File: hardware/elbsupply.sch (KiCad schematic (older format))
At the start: 84 parts, among them CON1 AVR-ISP-6, IC1 ATMEGA8-AI, P1 OUT_POS, P2 OUT_GND, P3 POWER_IN, Q1 KST2907A, SW1 SW_L, SW2 SW_R, SW3 SW_OE, SW4 SW_MD, U1 LM393, U2 TPS54331DDA, U3 LT1490, U4 LM358, U5 TS78L05CS, U6 LT3083, U7 LM334

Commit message: changed components to improve loop stability
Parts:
- added C?: 0.1uF, symbol C
- added R?: 10k, symbol R
- C14, C21: value 0.1uF -> 1uF
- C4: value 7pF -> 22pF
- R1: value 102k -> 100k
- R19: value 10k -> 1k
- R21, R7: value 1k -> 10k
- R26: value 68R -> 100R
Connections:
- wire segments 317 -> 324
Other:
- note added: "CC mode comparator\npulls output control voltage to \nGND when current exceeds \nset maximum"
- note added: "Current setting PWM DAC\nControl: 0...3V\nOutput: 0...3A"
- note added: "Tracking pre-regulator to minimize\npower dissipated in LT3083\nOutput voltage from 2V to 22V"
- note added: "Voltage setting PWM DAC"
- note removed: "CC mode comparator\npulls output control voltage to \nGND when current exceeds set maximum"
- note removed: "Current setting Filter & Buffer \nControl: 0...3V\nOutput: 0...3A"
- note removed: "Tracking pre-regulator to minimize\npower dissipated in output pass transistor\nOutput voltage from 2V to 22V"
- note removed: "Voltage setting Filter & Buffer\n"
- moved on the sheet: R19, RP1, RP3

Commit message: improved current limiting circuit, constant current LCD LED backlight driver
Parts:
- removed D5: SM6T27A, Diodes_SMD:Diode-SMB_Handsoldering, symbol TVS
- removed R19: 1k, Resistors_SMD:R_0603_HandSoldering, symbol R
- removed R23: 220, Resistors_SMD:R_0603_HandSoldering, symbol R
- removed U1: LM393, devthrash_KICAD:SO8, symbol LM393
- removed U3: LT1490, devthrash_KICAD:SO8, symbol LM358
- removed U6: LT3083, Pentawatts:Pentawatt_Neutral_Staggered_Verical_TO220-5-T05D, symbol LT3083
- added C?: 0.1uF, Capacitors_SMD:C_0603_HandSoldering, symbol C
- added C?: 1uF, symbol C
- added D?: SK54C, Diodes_SMD:Diode-SMC_Handsoldering, symbol DIODESCH
- added Q?: KST2907A, Housings_SOT-23_SOT-143_TSOT-6:SOT23_Handsoldering, symbol BC808-40
- added Q?: IRLML6302, symbol Q_PMOS_GSD
- added Q? (x2): 2N2222A, symbol Q_NPN_BEC
- added R?: 100, symbol R
- added R? (x2): 1k, symbol R
- added R?: 10k, symbol R
- added R?: 6R8, symbol R
- added R?: R, symbol R
- added U?: LT3083, symbol LT3083
- added U? (x4): LM358, symbol LM358
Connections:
- net labels added: ILIM, VCC
- net labels removed: V_control
- wire segments 324 -> 348
- no-connect marks 14 -> 16
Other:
- note added: "19VDC laptop power pack\ninput connector\n"
- note added: "Constant current\nLED backlight driver\n"
- note added: "Current sense resistor\n100mOhm, 3W, 1206\nCRA2512 R100E"
- note added: "Decoupling capacitors for \nop amps. Place close \nto supply pin of each LM358\n"
- note added: "Main loop regulator\nAv = 4V/V\nControl: 0...5V \nOutput: 0...15V"
- note added: "Tracking pre-regulator to minimize\npower dissipated in LT3083\nOutput voltage from 2V to 17V"
- note removed: "Current sense resistor\n10mOhm, 3W, 1206\nCRA2512 R100E"
- note removed: "Main loop regulator\nAv = 4V/V\nControl: 0...5V \nOutput: 0...20V"
- note removed: "Tracking pre-regulator to minimize\npower dissipated in LT3083\nOutput voltage from 2V to 22V"
- moved on the sheet: C10, C11, C13, C14, C17, C18, C19, C21, C22, C23, C?, D1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

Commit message: changed voltage measurement divider to new voltage range
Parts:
- removed R14, R16, R24, R25, R4, R5, R6: 10k, Resistors_SMD:R_0603_HandSoldering, symbol R
- removed RP4: 10k, devthrash_KICAD:YC164-Yageo, symbol R_PACK4
- added D?: SK54C, Diodes_SMD:Diode-SMC_Handsoldering, symbol DIODESCH
- added RP? (x2): 10k, devthrash_KICAD:YC164-Yageo, symbol R_PACK4
- added RV?: 10k, devthrash_KICAD:BITech-23B, symbol POT
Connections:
- wire segments 348 -> 353
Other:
- note added: "Voltage measurement\nvoltage divider\nRatio: 1/6\n\nCalibrate to 2.5V out at 15V in"
- note removed: "Voltage measurement\nvoltage divider\nRatio: 1/8"
- moved on the sheet: C10, C11, C12, C15, C16, C7, C9, CON1, D2, ENC1, R3, RP5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

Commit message: exchanged LT3083 for LM350, added negative rail and offset amplifiers
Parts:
- removed C10, C11, C12, C7, C9: 10nF, Capacitors_SMD:C_0603_HandSoldering, symbol C
- removed C25: 0.1uF, Capacitors_SMD:C_0603_HandSoldering, symbol C
- removed RP? (x2): 10k, devthrash_KICAD:YC164-Yageo, symbol R_PACK4
- removed U?: LT3083, symbol LT3083
- added C?: 100pF, symbol C
- added C?: 1uF, symbol C
- added C? (x2): 10uF, Capacitors_SMD:c_elec_4x4.5, symbol CP1
- added C?: 0.1uF, Capacitors_SMD:C_0603_HandSoldering, symbol C
- added D?: LM4040-AIM2.5, symbol ZENER
- added D?: DIODESCH, symbol DIODESCH
- added L?: 220uH, symbol INDUCTOR_SMALL
- added R?: 220, symbol R
- added R?: 1R2, symbol R
- added R?: 10k, Resistors_SMD:R_0603_HandSoldering, symbol R
- added RP? (x2): 10k, devthrash_KICAD:YC164-Yageo, symbol R_PACK4
- added U?: LM350T, symbol LM350T
- added U?: MC34063, symbol MC34063
- added U?: LM358, devthrash_KICAD:SO8, symbol LM358
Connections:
- net labels added: -5V, 2.5VREF
- net labels removed: +24V
- wire segments 353 -> 369
- no-connect marks 16 -> 15
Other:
- note added: "DC-DC inverter 19V in, -5V out\n\n"
- note added: "Main loop regulator\nAv = 3V/V\nControl: 0...5V \nOutput: 0...15V"
- note added: "User interface buttons,\nencoder and LEDs\n"
- note added: "Voltage setting PWM DAC\n0-5V PMW input is filtered and\nthen inverted to 0 to -5V"
- note removed: "Main loop regulator\nAv = 4V/V\nControl: 0...5V \nOutput: 0...15V"
- note removed: "Voltage setting PWM DAC"
- moved on the sheet: C15, C16, C17, C18, C19, C21, C22, C23, C?, CON1, D1, D2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

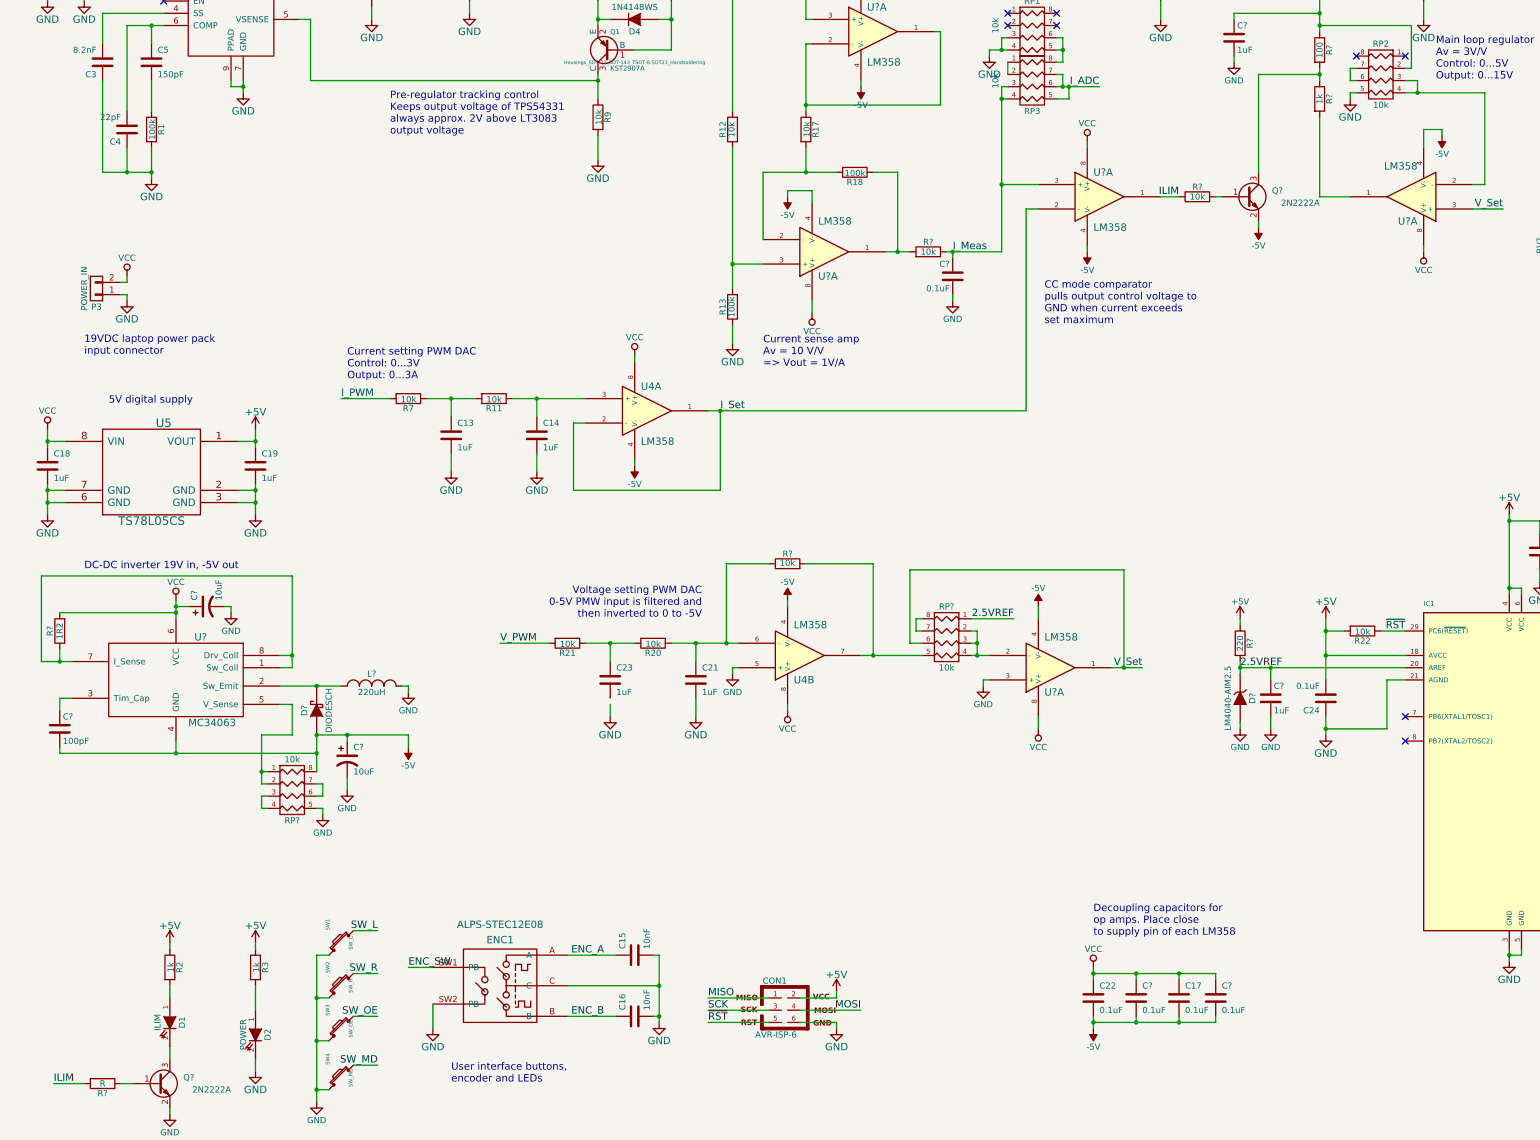
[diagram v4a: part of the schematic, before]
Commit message: extended negative rail to -7V, improved voltage adjustment
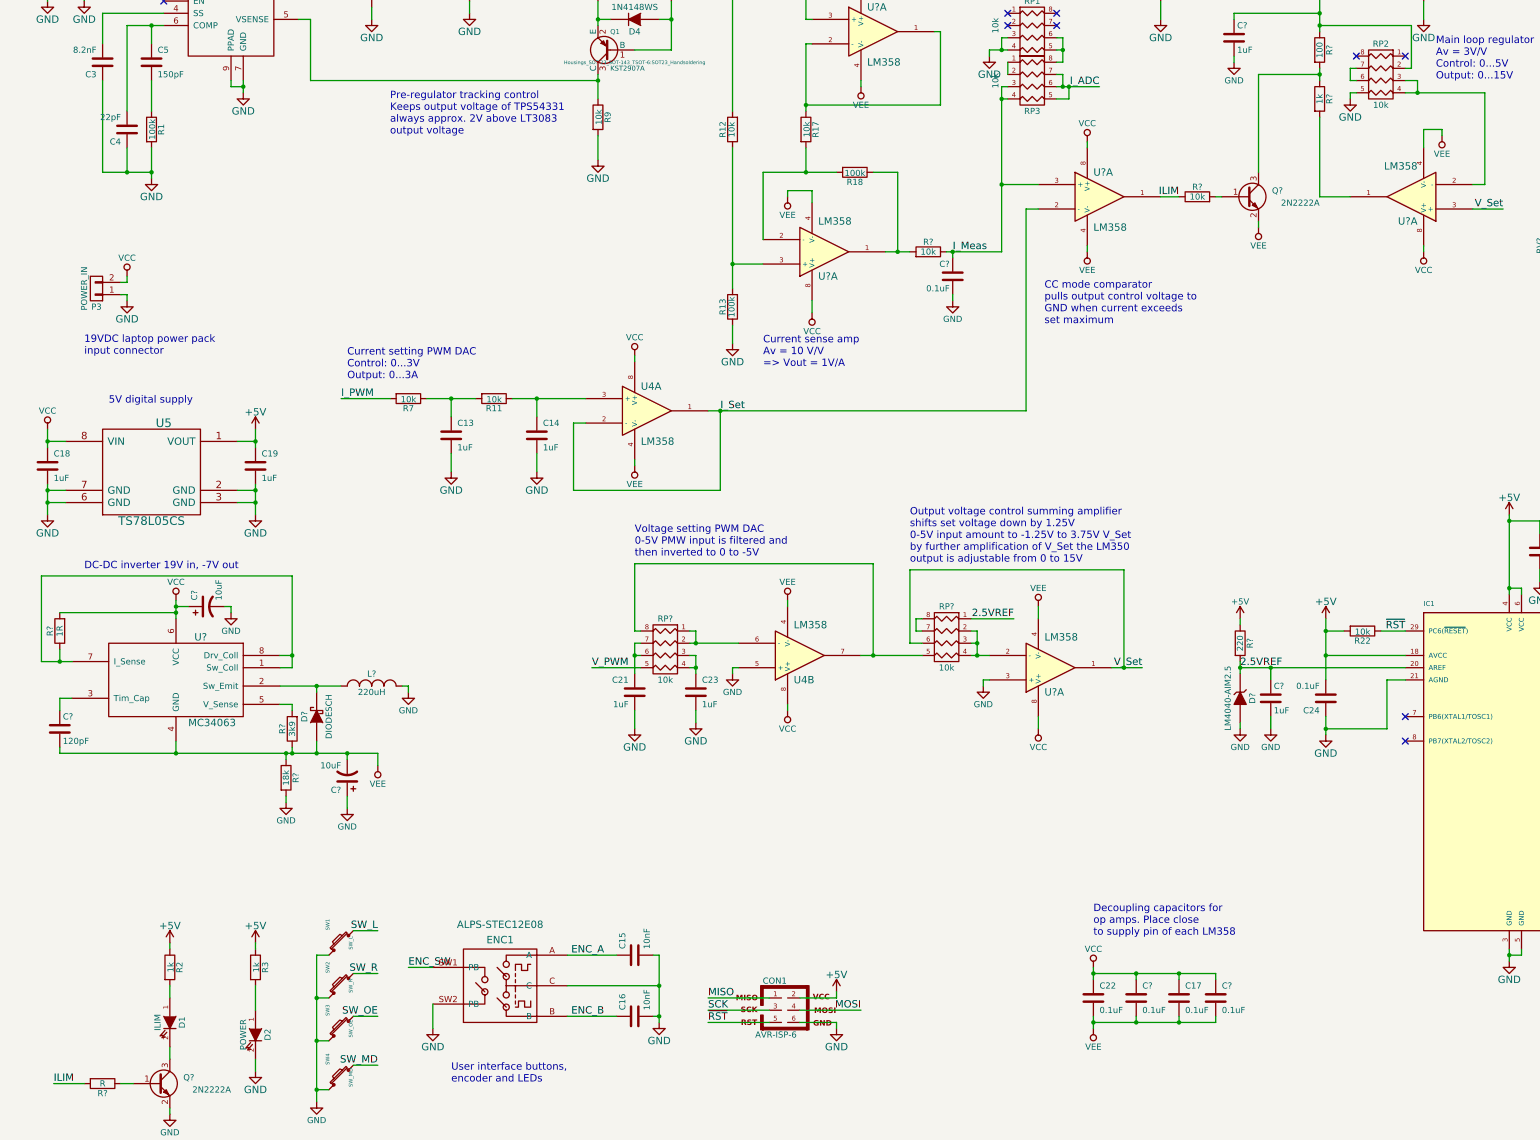
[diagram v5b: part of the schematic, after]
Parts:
- removed R20, R21, R?: 10k, Resistors_SMD:R_0603_HandSoldering, symbol R
- removed RP?: 10k, devthrash_KICAD:YC164-Yageo, symbol R_PACK4
- added R?: 3k9, symbol R
- added R?: 18k, symbol R
- added RP?: 10k, devthrash_KICAD:YC164-Yageo, symbol R_PACK4
- C?: value 100pF -> 120pF
- R?: value 1R2 -> 1R
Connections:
- net GND: now also C23.2, C?.1, R?.2; no longer C?.2
- net V_PWM: now also RP?.5 (R4)
- net at C21.1: now also RP?.6 (R3), RP?.7 (R2); no longer U4.6 (-)
- net at C23.1: now also RP?.3 (P3), RP?.4 (P4)
- net at RP?.5 (R4), U4.7: now also RP?.8 (R1)
- net at U?.5 (V_Sense): now also R?.2
- net -5V renamed VEE
- net VEE: now also C?.2, R?.1, R?.1; no longer C?.1
- new net: RP?.1 (P1), RP?.2 (P2), U4.6 (-)
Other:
- note added: "DC-DC inverter 19V in, -7V out\n\n"
- note added: "Output voltage control summing amplifier \nshifts set voltage down by 1.25V \n0-5V input amount to -1.25V to 3.75V V_Set \nby further amplification of V_Set the LM350 \noutput is adjustable from 0 to 15V"
- note removed: "DC-DC inverter 19V in, -5V out\n\n"
- moved on the sheet: C21, C23, C?, D?

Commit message: adjusted minimum load current, added heatsink
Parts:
- added HS?: HEATSINK V5640A, symbol HEATSINK
- R26: value 100R -> 10R
- R?: value 6R8 -> 10R
- R?: value R -> 10k
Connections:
- net GND: no longer R26.2, U7.2 (V-), U7.3 (V-), U7.6 (V-), U7.7 (V-)
- net VEE: now also R26.2, U7.2 (V-), U7.3 (V-), U7.6 (V-), U7.7 (V-)
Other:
- note added: "CC mode comparator\npulls output control voltage \nto GND when current \nexceeds set maximum"
- note added: "Constant current\nLED backlight driver\nI = 0.7V / 10R = 70mA"
- note added: "Decoupling capacitors for \nop amps. Place close \nto supply pin of each LM358\n0805 50V rated\n"
- note added: "LM334 ensures a minimum load\ncurrent for the LM350 for stable\n operation and adjustment down to 0V.\nI =67.6mV/10 Ohms = 7.76mA"
- note removed: "CC mode comparator\npulls output control voltage to \nGND when current exceeds \nset maximum"
- note removed: "Constant current\nLED backlight driver\n"
- note removed: "Decoupling capacitors for \nop amps. Place close \nto supply pin of each LM358\n"
- moved on the sheet: C13, C14, C15, C16, C17, C18, C19, C21, C22, C23, C24, C27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

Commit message: main control voltage op amp has voltage shifted down by 1.25V for LM350 0V output
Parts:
- removed RP? (x2): 10k, devthrash_KICAD:YC164-Yageo, symbol R_PACK4
- removed RV?: 10k, devthrash_KICAD:BITech-23B, symbol POT
- removed U4, U?: LM358, devthrash_KICAD:SO8, symbol LM358
- removed U? (x4): LM358, symbol LM358
- added R? (x2): 10k, symbol R
- added RP? (x3): 10k, devthrash_KICAD:YC164-Yageo, symbol R_PACK4
- added U? (x4): LM324, symbol LM324
- added U? (x2): LM358, symbol LM358
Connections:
- net 2.5VREF: now also RP?.1 (P1)
- net GND: now also C17.2, C22.2, C?.2, C?.2, R?.1, U?.3 (+), U?.3 (+); no longer RP2.5 (R4)
- net ILIM: now also U?.1
- net I_Meas: now also U?.3 (+)
- net I_Set: now also U?.1, U?.2 (-), U?.2 (-)
- net LIN_IN: now also U?.3 (+)
- net VCC: now also U?.4 (V+), U?.4 (V+), U?.4 (V+), U?.4 (V+), U?.8 (V+), U?.8 (V+); no longer C17.1, C?.1
- net VEE: now also C17.1, C?.1, U?.11 (V-), U?.11 (V-), U?.11 (V-), U?.11 (V-), U?.4 (V-), U?.4 (V-); no longer C17.2, C22.2, C?.2, C?.2
- net V_ADC: now also R?.2, R?.2
- net V_PWM: now also RP?.5 (R4)
- net V_Set: now also RP?.2 (P2), RP?.8 (R1), U?.1
- net at C21.1: now also RP?.3 (P3), RP?.4 (P4)
- net at C23.1: now also RP?.6 (R3), RP?.7 (R2)
- net at C14.1, R11.1: now also U?.3 (+)
- net at R18.1, R?.2: now also U?.1
- net at R17.2, R18.2: now also U?.2 (-)
- net at R12.1, R13.2: now also U?.3 (+)
- net at R17.1: now also U?.1, U?.2 (-)
- net at C?.1, R?.1, U?.1 (ADJ): now also RP2.7 (R2); no longer RP2.2 (P2)
- net at RP2.3 (P3): now also RP2.2 (P2); no longer RP2.4 (P4)
- net at RP2.6 (R3): now also RP2.5 (R4); no longer RP2.7 (R2)
- net at RP5.4 (P4): now also R?.1
- net at R?.2: now also U?.1
- new net: RP2.4 (P4), RP?.6 (R3), RP?.7 (R2), U?.2 (-)
- new net: RP?.2 (P2), RP?.3 (P3)
- new net: RP?.4 (P4), RP?.5 (R4)
- new net: RP?.5 (R4), RP?.6 (R3)
- new net: RP?.7 (R2), RP?.8 (R1)
- new net: RP?.3 (P3), RP?.4 (P4)
- new net: RP?.1 (P1), RP?.2 (P2), U?.2 (-)
- no-connect marks 15 -> 17
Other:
- note added: "Decoupling capacitors for \nop amps. Place close \nto supply pin of each op amp\n0805 50V rated\n"
- note added: "Main loop regulator\nAv = 3V/V\nInput: 0...-5V \nOutput: -1.25...13.75V"
- note added: "Voltage measurement\nvoltage divider\nRatio: 1/6"
- note added: "Voltage setting PWM DAC\nVoltage is inverted \n0 to 5V --> 0 to -5V out"
- note removed: "Decoupling capacitors for \nop amps. Place close \nto supply pin of each LM358\n0805 50V rated\n"
- note removed: "Main loop regulator\nAv = 3V/V\nControl: 0...5V \nOutput: 0...15V"
- note removed: "Output voltage control summing amplifier \nshifts set voltage down by 1.25V \n0-5V input amount to -1.25V to 3.75V V_Set \nby further amplification of V_Set the LM350 \noutput is adjustable from 0 to 15V"
- note removed: "Voltage measurement\nvoltage divider\nRatio: 1/6\n\nCalibrate to 2.5V out at 15V in"
- note removed: "Voltage setting PWM DAC\n0-5V PMW input is filtered and\nthen inverted to 0 to -5V"
- moved on the sheet: C13, C14, C15, C16, C17, C21, C23, C24, C27, C?, CON1, D1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

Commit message: changed tracking preregulator output tracking and compensation
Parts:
- removed C20: 10uF, Capacitors_SMD:c_elec_4x4.5, symbol CP1
- added R?: 33k, Resistors_SMD:R_0603_HandSoldering, symbol R
- R8: value 18k -> 33k
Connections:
- net GND: now also Q?.2 (E)
- net VEE: no longer Q?.2 (E)
- net at C5.2: now also R?.1; no longer R1.1
- new net: R1.1, R?.2
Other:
- note added: "Pre-regulator tracking control\nKeeps output voltage of TPS54331\nalways approx. 3V3 above LM350\noutput voltage"
- note added: "Voltage setting PWM DAC\nVoltage output is inverted \n0 to 5V in --> 0 to -5V out"
- note removed: "Pre-regulator tracking control\nKeeps output voltage of TPS54331\nalways approx. 2V above LT3083\noutput voltage"
- note removed: "Voltage setting PWM DAC\nVoltage is inverted \n0 to 5V --> 0 to -5V out"
- moved on the sheet: C26, R1, R26, R?, RP5, U7
